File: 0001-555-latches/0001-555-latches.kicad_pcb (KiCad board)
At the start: 2 copper layers, 13 parts, among them J1 DC_IN, J2 ASTBL_OUT, J3 BSTBL_OUT, J4 MSTBL_OUT, SW1 SW_Push, SW2 SW_Push, SW3 SW_Push, U1 NE555P, U2 NE555P, U3 NE555P

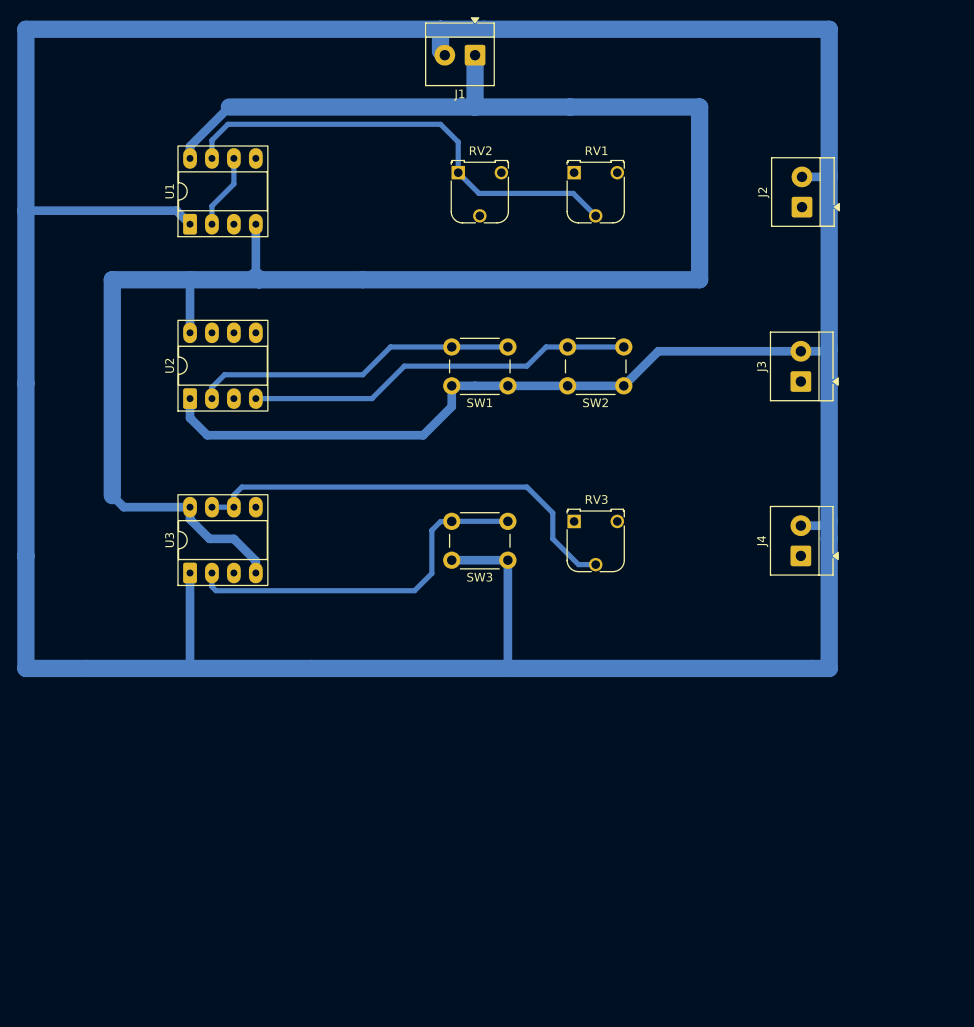
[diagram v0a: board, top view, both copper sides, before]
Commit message: All PCB connections
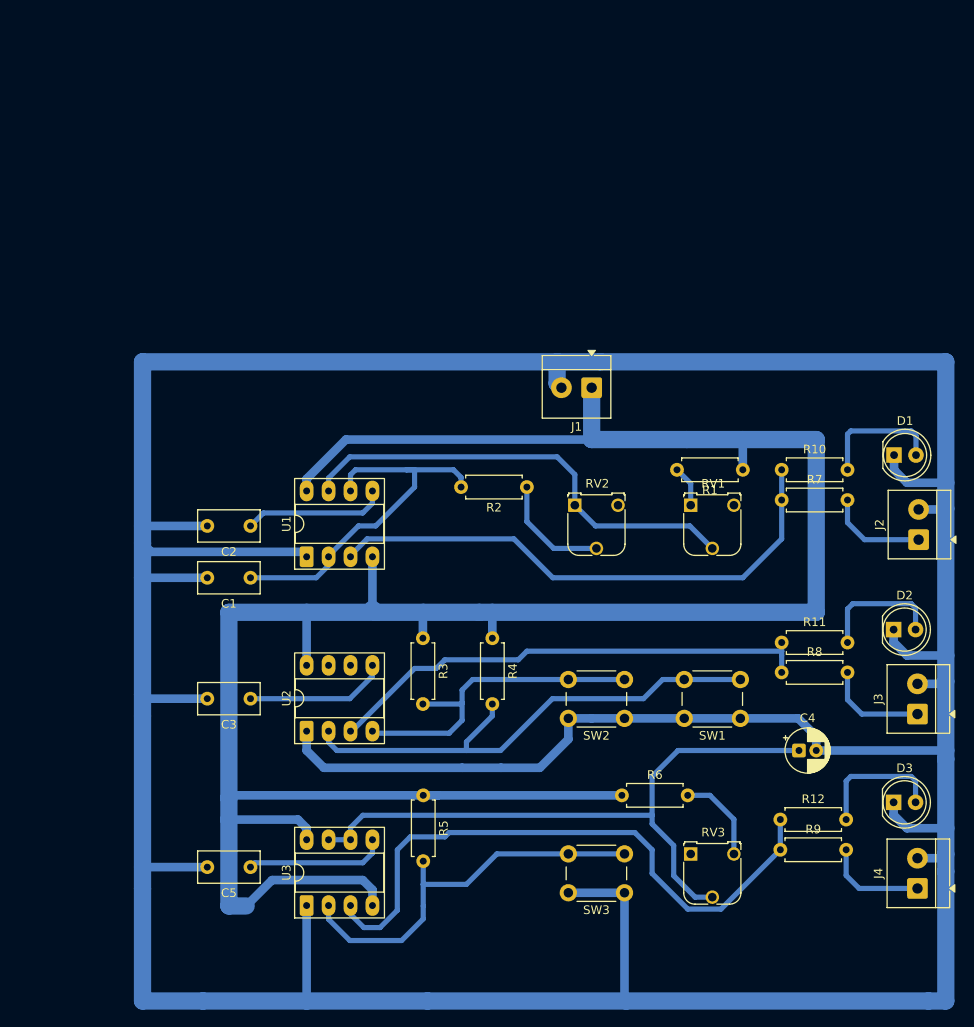
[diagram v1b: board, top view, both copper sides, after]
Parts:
- added C1: 470nF, Capacitor_THT:C_Rect_L7.0mm_W3.5mm_P5.00mm, F.Cu at (116.0, 88.5)
- added C2: 10nF, Capacitor_THT:C_Rect_L7.0mm_W3.5mm_P5.00mm, F.Cu at (116.0, 82.5)
- added C3: 10nF, Capacitor_THT:C_Rect_L7.0mm_W3.5mm_P5.00mm, F.Cu at (116.0, 102.5)
- added C4: 22uF, Capacitor_THT:CP_Radial_D5.0mm_P2.00mm, F.Cu at (179.5, 108.5)
- added C5: 10nF, Capacitor_THT:C_Rect_L7.0mm_W3.5mm_P5.00mm, F.Cu at (116.0, 122.0)
- added D1: RED, LED_THT:LED_D5.0mm, F.Cu at (190.5, 74.3)
- added D2: GREEN, LED_THT:LED_D5.0mm, F.Cu at (190.5, 94.5)
- added D3: YELLOW, LED_THT:LED_D5.0mm, F.Cu at (190.5, 114.5)
- added R1: 1k, Resistor_THT:R_Axial_DIN0207_L6.3mm_D2.5mm_P7.62mm_Horizontal, F.Cu at (173.0, 76.0)
- added R10: 10k, Resistor_THT:R_Axial_DIN0207_L6.3mm_D2.5mm_P7.62mm_Horizontal, F.Cu at (177.5, 76.0)
- added R11: 10k, Resistor_THT:R_Axial_DIN0207_L6.3mm_D2.5mm_P7.62mm_Horizontal, F.Cu at (177.5, 96.0)
- added R12: 10k, Resistor_THT:R_Axial_DIN0207_L6.3mm_D2.5mm_P7.62mm_Horizontal, F.Cu at (177.3, 116.5)
- added R2: 1k, Resistor_THT:R_Axial_DIN0207_L6.3mm_D2.5mm_P7.62mm_Horizontal, F.Cu at (148.0, 78.0)
- added R3: 10k, Resistor_THT:R_Axial_DIN0207_L6.3mm_D2.5mm_P7.62mm_Horizontal, F.Cu at (136.0, 95.5)
- added R4: 10k, Resistor_THT:R_Axial_DIN0207_L6.3mm_D2.5mm_P7.62mm_Horizontal, F.Cu at (144.0, 95.5)
- added R5: 10k, Resistor_THT:R_Axial_DIN0207_L6.3mm_D2.5mm_P7.62mm_Horizontal, F.Cu at (136.0, 113.7)
- added R6: 1k, Resistor_THT:R_Axial_DIN0207_L6.3mm_D2.5mm_P7.62mm_Horizontal, F.Cu at (159.0, 113.7)
- added R7: 1k, Resistor_THT:R_Axial_DIN0207_L6.3mm_D2.5mm_P7.62mm_Horizontal, F.Cu at (177.5, 79.5)
- added R8: 1k, Resistor_THT:R_Axial_DIN0207_L6.3mm_D2.5mm_P7.62mm_Horizontal, F.Cu at (177.5, 99.5)
- added R9: 1k, Resistor_THT:R_Axial_DIN0207_L6.3mm_D2.5mm_P7.62mm_Horizontal, F.Cu at (177.3, 120.0)
- moved SW1 47.0 mm to (172.7, 104.8)
- moved J1 40.8 mm to (155.5, 66.5)
- moved J2 40.8 mm to (193.4, 84.1)
- moved J3 40.8 mm to (193.2, 104.3)
- moved J4 40.8 mm to (193.2, 124.5)
- moved RV1 40.8 mm to (167.0, 80.1)
- moved RV2 40.8 mm to (153.6, 80.1)
- moved RV3 40.8 mm to (167.0, 120.5)
- moved SW3 40.8 mm to (159.3, 125.0)
- moved U2 40.8 mm to (122.5, 106.3)
- moved U3 40.8 mm to (122.5, 126.4)
- moved U1 40.8 mm to (122.5, 86.1)
- moved SW2 38.5 mm to (159.3, 104.8)
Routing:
- net VCC: track 216.0 -> 289.1 mm
- net Net-(U3-Q): track 0.00 -> 71.7 mm
- net Net-(U1-Q): track 0.00 -> 62.6 mm
- net GND: track 476.3 -> 534.7 mm
- net Net-(U2-Q): track 0.00 -> 57.2 mm
- net Net-(U1-THR): track 8.67 -> 43.3 mm
- net Net-(U3-DIS): track 51.7 -> 75.7 mm
- net Net-(U2-TR): track 37.5 -> 59.4 mm
- net Net-(U1-CV): track 0.00 -> 16.6 mm
- net Net-(U2-CV): track 0.00 -> 16.4 mm
- net Net-(U3-CV): track 0.00 -> 16.3 mm
- net Net-(D3-A): track 0.00 -> 15.4 mm
- net Net-(D2-A): track 0.00 -> 14.7 mm
- net Net-(D1-A): track 0.00 -> 14.7 mm
- net Net-(R2-Pad1): track 0.00 -> 13.3 mm
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
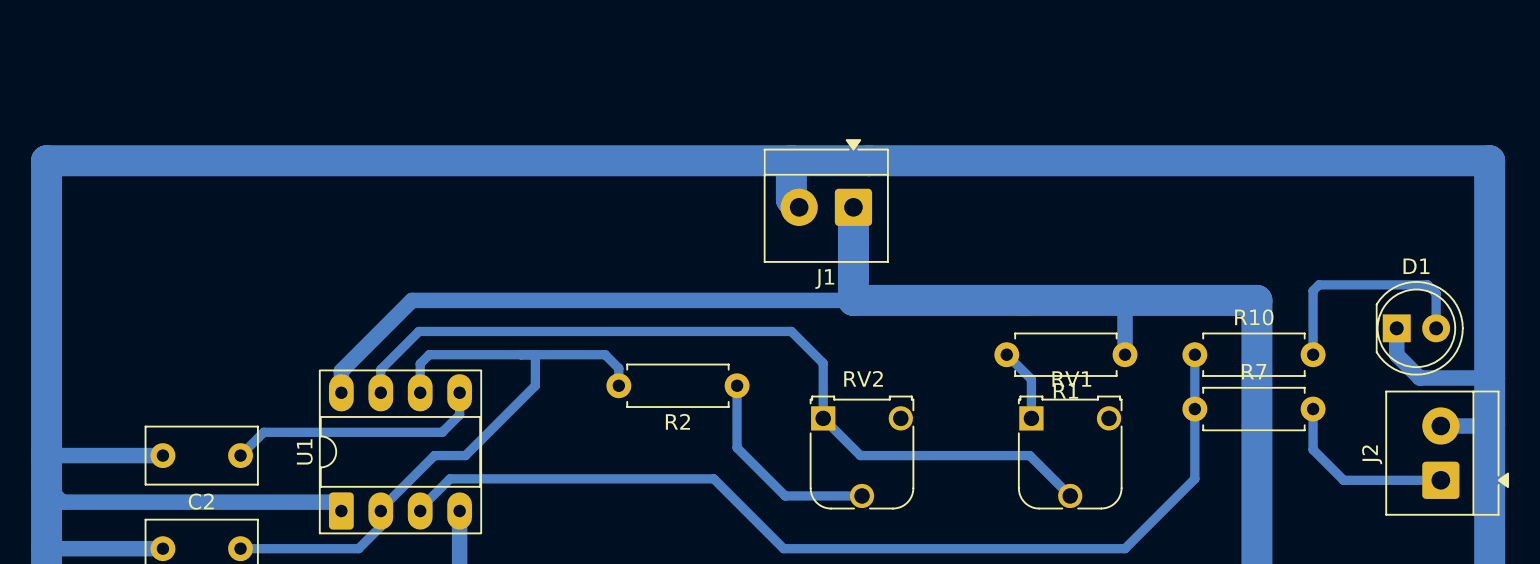
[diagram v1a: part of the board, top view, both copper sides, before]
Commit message: Replace DC_IN screw connector with DC jack
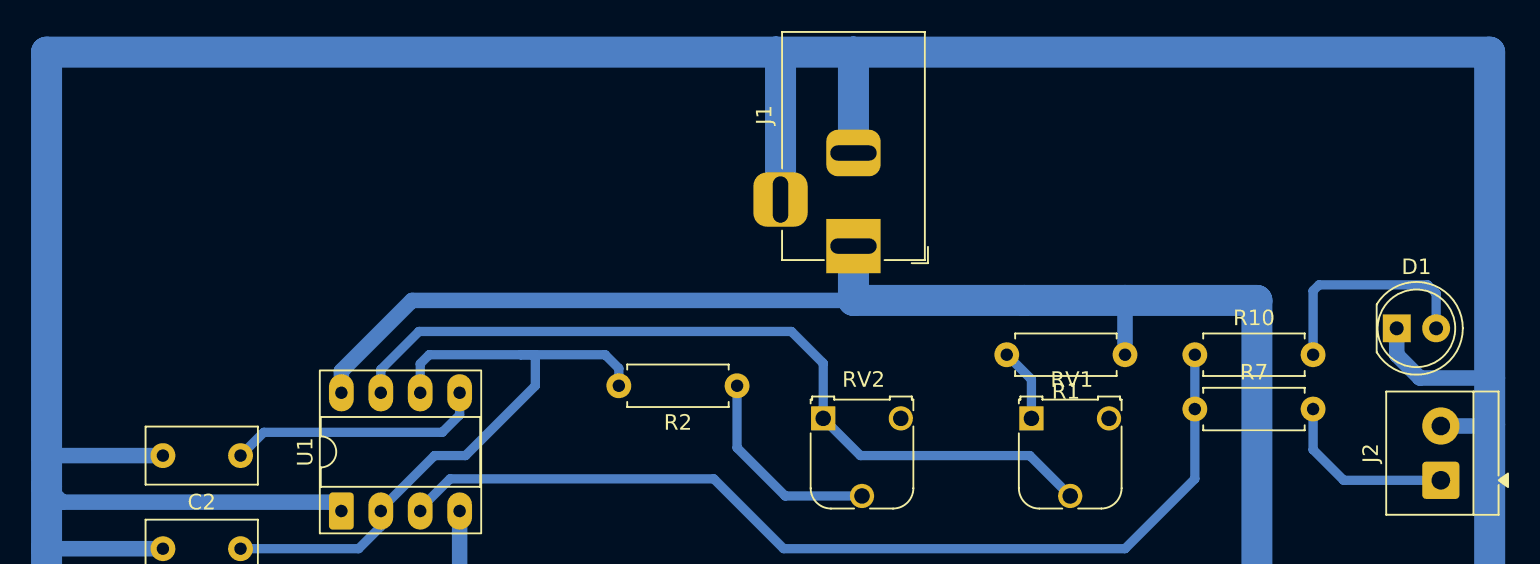
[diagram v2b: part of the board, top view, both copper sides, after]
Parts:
- J1: footprint TerminalBlock_4Ucon:TerminalBlock_4Ucon_1x02_P3.50mm_Horizontal -> Connector_BarrelJack:BarrelJack_Horizontal
- moved J1 2.50 mm to (155.5, 69.0), turned to -90 degrees
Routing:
- net GND: track 534.7 -> 561.6 mm
- net VCC: track 289.1 -> 287.1 mm

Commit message: PCB compression
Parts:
- moved R7 11.4 mm to (166.7, 83.3)
- moved R8 11.1 mm to (166.7, 102.3)
- moved R12 10.9 mm to (166.6, 114.8)
- moved D3 10.9 mm to (179.7, 112.8)
- moved J4 10.9 mm to (182.4, 122.8)
- moved R9 10.9 mm to (166.6, 121.3)
- moved D1 10.9 mm to (179.7, 75.6)
- moved J2 10.9 mm to (182.6, 85.4)
- moved R10 10.9 mm to (166.7, 77.3)
- moved D2 10.8 mm to (179.7, 94.3)
- moved J3 10.8 mm to (182.4, 104.1)
- moved R11 10.8 mm to (166.7, 95.8)
- moved SW1 10.4 mm to (162.3, 104.6)
- moved RV3 10.3 mm to (156.8, 118.8)
- moved RV1 10.2 mm to (156.8, 81.4)
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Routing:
- net GND: track 561.6 -> 461.9 mm
- net VCC: track 287.1 -> 253.3 mm
- net Net-(D3-A): track 15.4 -> 11.3 mm
- net Net-(U3-TR): track 46.1 -> 49.6 mm
- net /BSTBL_OUT: track 12.0 -> 8.91 mm
- net /MSTBL_OUT: track 11.9 -> 8.87 mm
- net Net-(U3-DIS): track 75.7 -> 73.2 mm
- net /ASTBL_OUT: track 11.7 -> 9.17 mm
- net Net-(U2-TR): track 59.4 -> 57.2 mm
- net Net-(U3-Q): track 71.7 -> 73.8 mm
- net Net-(U1-DIS): track 53.4 -> 51.4 mm
- net Net-(U2-Q): track 57.2 -> 58.8 mm
- net Net-(U1-THR): track 43.3 -> 44.6 mm
- net Net-(U1-Q): track 62.6 -> 61.6 mm
- net Net-(R6-Pad2): track 10.5 -> 11.4 mm

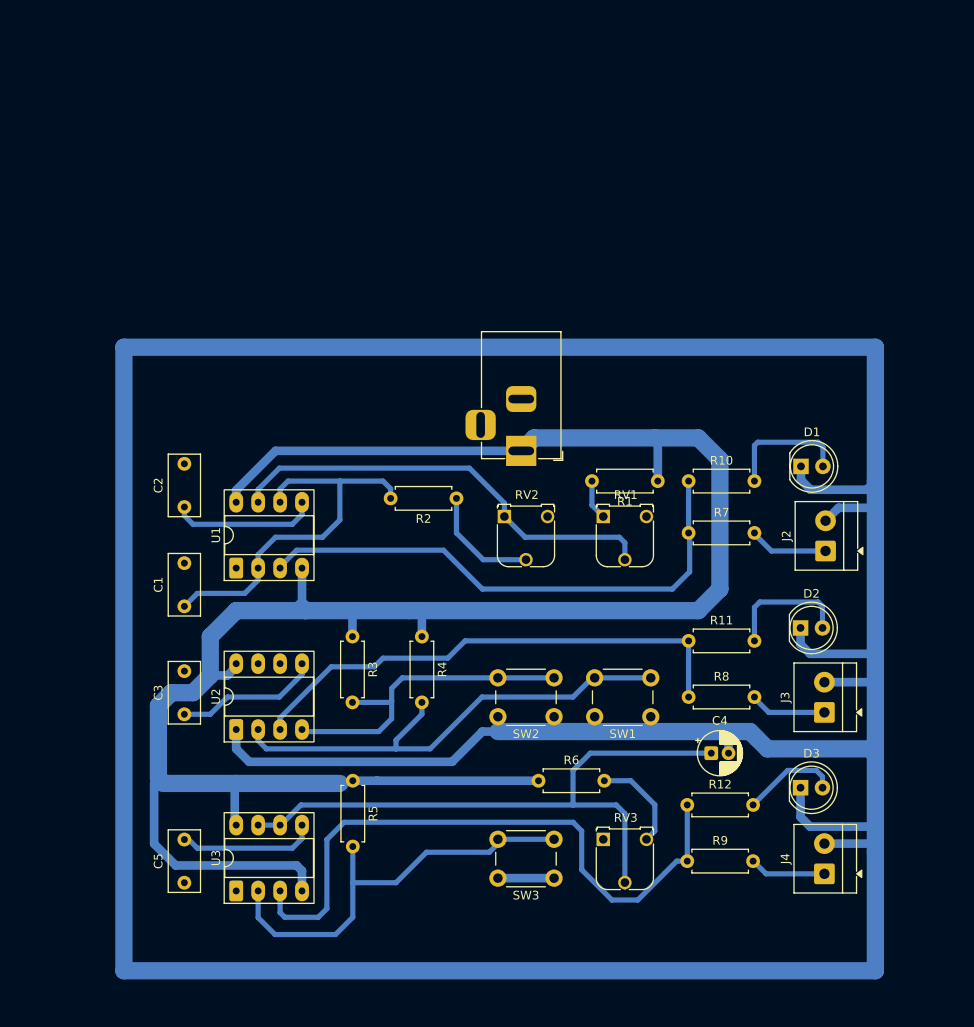
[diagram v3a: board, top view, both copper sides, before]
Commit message: Optimizing tracks
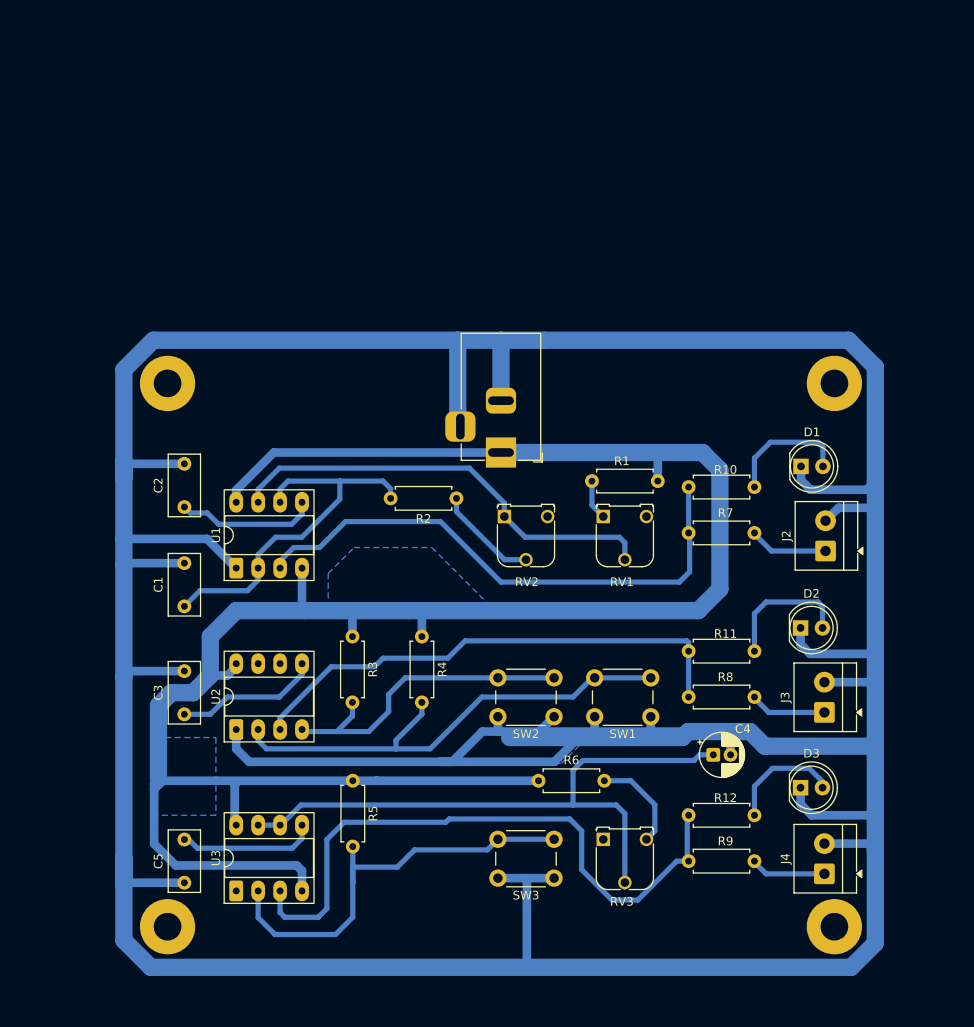
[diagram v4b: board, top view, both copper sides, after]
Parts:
- added REF**: MountingHole_3.2mm_M3_Pad, MountingHole:MountingHole_3.2mm_M3_Pad, F.Cu at (183.6, 66.0)
- added REF**: MountingHole_3.2mm_M3_Pad, MountingHole:MountingHole_3.2mm_M3_Pad, F.Cu at (106.4, 128.9)
- added REF**: MountingHole_3.2mm_M3_Pad, MountingHole:MountingHole_3.2mm_M3_Pad, F.Cu at (106.4, 66.0)
- added REF**: MountingHole_3.2mm_M3_Pad, MountingHole:MountingHole_3.2mm_M3_Pad, F.Cu at (183.6, 128.9)
- moved J1 2.35 mm to (145.0, 74.0)
- moved R12 1.21 mm to (166.7, 116.0)
- moved R11 1.19 mm to (166.7, 97.0)
- moved R10 0.69 mm to (166.7, 78.0)
- moved C4 0.30 mm to (169.6, 109.0)
- moved R9 0.16 mm to (166.7, 121.3)
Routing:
- net GND: track 461.9 -> 584.1 mm
- net Net-(D3-A): track 11.3 -> 13.4 mm
- net Net-(U1-Q): track 61.6 -> 63.4 mm
- net VCC: track 253.3 -> 251.8 mm
- net Net-(R2-Pad1): track 13.3 -> 11.9 mm
- net Net-(U1-THR): track 44.6 -> 43.2 mm
- net Net-(U2-R): track 38.5 -> 37.2 mm
- net Net-(U3-TR): track 49.6 -> 50.3 mm
- net Net-(D2-A): track 14.7 -> 15.5 mm
- net Net-(U1-CV): track 16.9 -> 16.3 mm
- added copper zone on B.Cu, net GND
- added copper zone on B.Cu, net VCC
